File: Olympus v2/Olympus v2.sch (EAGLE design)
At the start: 170 parts, among them J1 HEADER_10P_0.05, Q1 BSS138, Q10 BSS138, Q11 BSS138, Q12 BSS138, Q2 BSS138, Q3 BSS138, Q4 BSS138, Q5 BSS138, Q6 BSS138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

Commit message: I updated Olympus by changing the USB pins, the GPIO LEDS, and updated the Hermes, Hephaestus, and Iris pinouts and connections to the microcontroller.  I also added pull down resistors on theLEDS.
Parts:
- removed JP63, JP64, JP65, JP71: (no value), pinhead:PINHD-1X2
- removed LED10, LED11, LED12, LED9: (no value), led:LEDCHIP-LED0603
- removed Q10, Q11, Q12, Q9: BSS138, transistor-small-signal:BSS123
- removed R11, R12, R13, R20: 100, resistor:R-US_R0603
- added JP88: (no value), pinhead:PINHD-1X2
- added R24, R25, R26, R27, R32, R33, R34, R35: 10k, resistor:R-US_R0603
- R10, R3, R4, R5, R6, R7, R8, R9: value 100 -> 1k
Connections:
- removed net HEPHAESTUS_GPIO: JP32.1, SV9.9
- removed net HERA_SONAR6: JP42.2, SV12.2
- removed net LED10_A: LED10.A, R12.1
- removed net LED10_C: LED10.C, Q10.D
- removed net LED10_G: JP64.1, Q10.G
- removed net LED11_A: LED11.A, R13.1
- removed net LED11_C: LED11.C, Q11.D
- removed net LED11_G: JP65.1, Q11.G
- removed net LED12_A: LED12.A, R20.1
- removed net LED12_C: LED12.C, Q12.D
- removed net LED12_G: JP71.1, Q12.G
- removed net LED9_A: LED9.A, R11.1
- removed net LED9_C: LED9.C, Q9.D
- removed net LED9_G: JP63.1, Q9.G
- removed net OLYMPUS_GPIO10: JP41.2, JP64.2
- removed net OLYMPUS_GPIO11: JP49.2, JP65.2
- removed net OLYMPUS_GPIO12: JP70.2, JP71.2
- removed net OLYMPUS_GPIO9: JP40.2, JP63.2
- new net ENABLE: SV7.7
- new net HEPH_BRAKE_DIR: JP21.1
- new net HEPH_BRAKE_DIR2: JP40.2
- new net HEPH_DIR_B: SV10.1
- new net HEPH_DIR_S: SV9.7
- new net HEPH_FAULT_B: JP38.2, SV10.4
- new net HEPH_FAULT_S: JP37.2, SV9.10
- new net HEPH_GPIO_B: SV10.3
- new net HEPH_GPIO_S: SV9.9
- new net HEPH_PWM_B: SV10.2
- new net HEPH_PWM_BRAKE: JP8.1
- new net HEPH_PWM_S: SV9.8
- new net HEPH_STR_DIR2: JP41.2
- new net HERMES_PED_DET: JP5.1, SV7.8
- new net IRIS_CLOCK: JP6.1, SV3.10
- new net IRIS_DATA: JP22.1, SV3.9
- new net N$2: JP88.2
- new net OLYMPUS_USBDM: JP31.1
- new net OLYMP_JTAG_SWO: JP20.1
- net DIONYSUS_BRD_EN: no longer JP18.1
- net GND: now also R24.2, R25.2, R26.2, R27.2, R32.2, R33.2, R34.2, R35.2; no longer Q10.S, Q11.S, Q12.S, Q9.S
- net HEPHAESTUS_DIR: no longer SV9.7
- net HEPHAESTUS_SPD: no longer SV9.8
- net HERA_HALL2: now also JP42.2; no longer JP31.1
- net HERMES_AUTOMAN: no longer SV7.7
- net LED1_G: now also R24.1
- net LED2_G: now also R25.1
- net LED3_G: now also R26.1
- net LED4_G: now also R27.1
- net LED5_G: now also R32.1
- net LED6_G: now also R33.1
- net LED7_G: now also R34.1
- net LED8_G: now also R35.1
- net MCU_BOOT0: now also JP88.1
- net OLYMPUS_GPIO1: now also JP11.1; no longer JP5.1
- net OLYMPUS_GPIO2: now also JP12.1; no longer JP6.1
- net OLYMPUS_GPIO3: now also JP13.1; no longer JP8.1
- net OLYMPUS_GPIO4: now also JP18.1; no longer JP20.1
- net OLYMPUS_GPIO5: now also JP49.2; no longer JP21.1
- net OLYMPUS_GPIO6: now also JP70.2; no longer JP22.1
- net OLYMPUS_GPIO7: no longer JP37.2
- net OLYMPUS_GPIO8: no longer JP38.2
- net OLYMPUS_USBDN: no longer JP12.1
- net OLYMPUS_USBDP: now also JP32.1; no longer JP13.1
- net OLYMPUS_USBID: no longer JP11.1
- net PP5V: no longer R11.2, R12.2, R13.2, R20.2
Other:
- moved on the sheet: JP55, JP56, JP57, JP58, JP59, JP60, JP61, JP62, LED1, LED2, LED3, LED4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

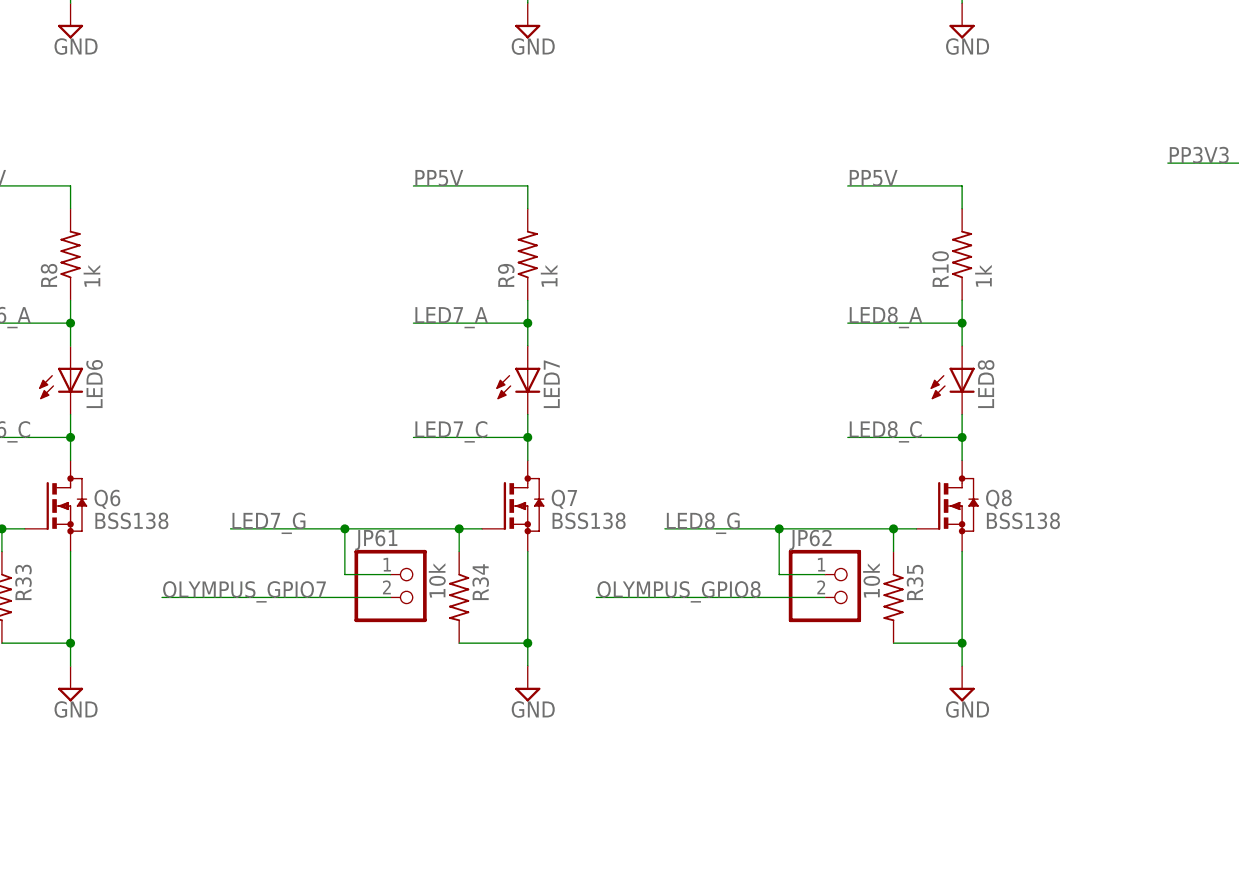
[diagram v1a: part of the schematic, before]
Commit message: I updated Olympus by changing the USB pins, the GPIO LEDS, and updated the Hermes, Hephaestus, and Iris pinouts and connections to the microcontroller.  I also added pull down resistors on theLEDS.
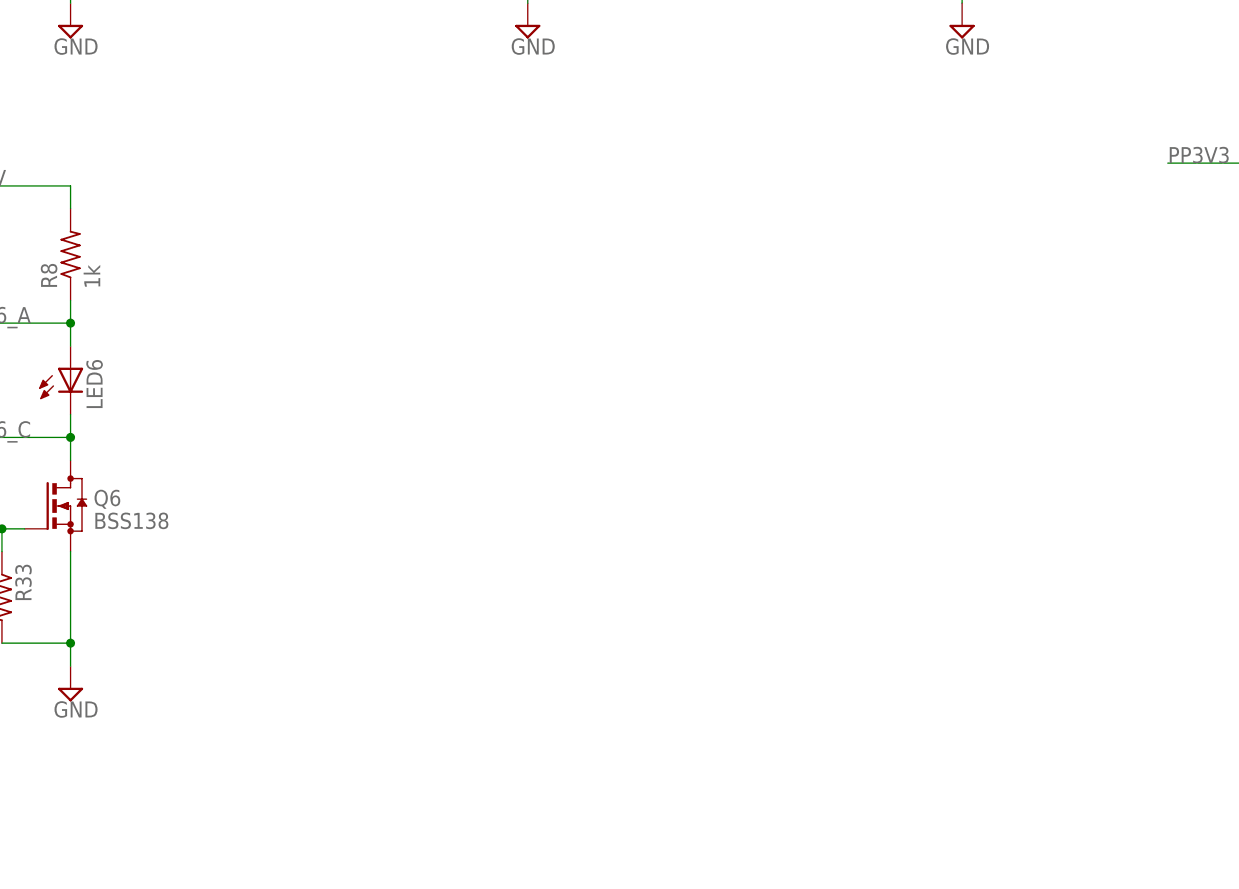
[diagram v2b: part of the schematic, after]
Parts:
- removed JP61, JP62: (no value), pinhead:PINHD-1X2
- removed LED7, LED8: (no value), led:LEDCHIP-LED0603
- removed Q7, Q8: BSS138, transistor-small-signal:BSS123
- removed R10, R9: 1k, resistor:R-US_R0603
- removed R34, R35: 10k, resistor:R-US_R0603
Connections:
- removed net LED7_A: LED7.A, R9.1
- removed net LED7_C: LED7.C, Q7.D
- removed net LED7_G: JP61.1, Q7.G, R34.1
- removed net LED8_A: LED8.A, R10.1
- removed net LED8_C: LED8.C, Q8.D
- removed net LED8_G: JP62.1, Q8.G, R35.1
- removed net OLYMPUS_GPIO7: JP61.2
- removed net OLYMPUS_GPIO8: JP62.2
- net GND: no longer Q7.S, Q8.S, R34.2, R35.2
- net PP5V: no longer R10.2, R9.2
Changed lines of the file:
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@@
 <part name="SUPPLY24" library="supply2" deviceset="GND" device=""/>
 <part name="JP60" library="pinhead" deviceset="PINHD-1X2" device=""/>
-<part name="LED7" library="led" deviceset="LED" device="CHIP-LED0603">
-<attribute name="DIGI" value="732-4966-1-ND"/>
-</part>
-<part name="R9" library="resistor" deviceset="R-US_" device="R0603" value="1k"/>
-<part name="Q7" library="transistor-small-signal" deviceset="BSS123" device="" value="BSS138">
-<attribute name="DIGI" value="BSS138CT-ND"/>
-</part>
-<part name="SUPPLY25" library="supply2" deviceset="GND" device=""/>
-<part name="JP61" library="pinhead" deviceset="PINHD-1X2" device=""/>
-<part name="LED8" library="led" deviceset="LED" device="CHIP-LED0603">
-<attribute name="DIGI" value="732-4966-1-ND"/>
-</part>
-<part name="R10" library="resistor" deviceset="R-US_" device="R0603" value="1k"/>
-<part name="Q8" library="transistor-small-signal" deviceset="BSS123" device="" value="BSS138">
-<attribute name="DIGI" value="BSS138CT-ND"/>
-</part>
-<part name="SUPPLY26" library="supply2" deviceset="GND" device=""/>
-<part name="JP62" library="pinhead" deviceset="PINHD-1X2" device=""/>
 <part name="L1" library="rcl" deviceset="L-US" device="L0201">
 <attribute name="DIGI" value="445-15755-1-ND"/>
@@
 <part name="R32" library="resistor" deviceset="R-US_" device="R0603" value="10k"/>
 <part name="R33" library="resistor" deviceset="R-US_" device="R0603" value="10k"/>
-<part name="R34" library="resistor" deviceset="R-US_" device="R0603" value="10k"/>
-<part name="R35" library="resistor" deviceset="R-US_" device="R0603" value="10k"/>
 <part name="U$1" library="Olympus" deviceset="NC" device=""/>
 </parts>
@@
 <instance part="SUPPLY24" gate="GND" x="454.66" y="190.5"/>
 <instance part="JP60" gate="G$1" x="441.96" y="200.66"/>
-<instance part="LED7" gate="G$1" x="505.46" y="226.06">
-<attribute name="DIGI" x="505.46" y="226.06" size="1.778" layer="96" display="off"/>
-</instance>
-<instance part="R9" gate="G$1" x="505.46" y="238.76" rot="R90"/>
-<instance part="Q7" gate="G$1" x="505.46" y="210.82">
-<attribute name="DIGI" x="505.46" y="210.82" size="1.778" layer="96" display="off"/>
-</instance>
-<instance part="SUPPLY25" gate="GND" x="505.46" y="190.5"/>
-<instance part="JP61" gate="G$1" x="492.76" y="200.66"/>
-<instance part="LED8" gate="G$1" x="553.72" y="226.06">
-<attribute name="DIGI" x="553.72" y="226.06" size="1.778" layer="96" display="off"/>
-</instance>
-<instance part="R10" gate="G$1" x="553.72" y="238.76" rot="R90"/>
-<instance part="Q8" gate="G$1" x="553.72" y="210.82">
-<attribute name="DIGI" x="553.72" y="210.82" size="1.778" layer="96" display="off"/>
-</instance>
-<instance part="SUPPLY26" gate="GND" x="553.72" y="190.5"/>
-<instance part="JP62" gate="G$1" x="541.02" y="200.66"/>
 <instance part="L1" gate="G$1" x="259.08" y="68.58" rot="R90">
 <attribute name="DIGI" x="259.08" y="68.58" size="1.778" layer="96" rot="R90" display="off"/>
@@
 <instance part="R32" gate="G$1" x="393.7" y="200.66" rot="R270"/>
 <instance part="R33" gate="G$1" x="447.04" y="200.66" rot="R270"/>
-<instance part="R34" gate="G$1" x="497.84" y="200.66" rot="R270"/>
-<instance part="R35" gate="G$1" x="546.1" y="200.66" rot="R270"/>
 <instance part="U$1" gate="G$1" x="523.24" y="43.18"/>
 </instances>
@@
 <wire x1="325.12" y1="160.02" x2="355.6" y2="160.02" width="0.1524" layer="91"/>
 <label x="355.6" y="160.02" size="1.778" layer="95" rot="MR0"/>
-</segment>
-</net>
-<net name="OLYMPUS_GPIO7" class="0">
-<segment>
-<pinref part="JP61" gate="G$1" pin="2"/>
-<wire x1="490.22" y1="200.66" x2="464.82" y2="200.66" width="0.1524" layer="91"/>
-<label x="464.82" y="200.66" size="1.778" layer="95"/>
-</segment>
-</net>
-<net name="OLYMPUS_GPIO8" class="0">
-<segment>
-<pinref part="JP62" gate="G$1" pin="2"/>
-<wire x1="538.48" y1="200.66" x2="513.08" y2="200.66" width="0.1524" layer="91"/>
-<label x="513.08" y="200.66" size="1.778" layer="95"/>
 </segment>
 </net>
@@
 <wire x1="447.04" y1="195.58" x2="454.66" y2="195.58" width="0.1524" layer="91"/>
 <junction x="454.66" y="195.58"/>
-</segment>
-<segment>
-<pinref part="Q7" gate="G$1" pin="S"/>
-<wire x1="505.46" y1="205.74" x2="505.46" y2="195.58" width="0.1524" layer="91"/>
-<pinref part="SUPPLY25" gate="GND" pin="GND"/>
-<pinref part="R34" gate="G$1" pin="2"/>
-<wire x1="505.46" y1="195.58" x2="505.46" y2="193.04" width="0.1524" layer="91"/>
-<wire x1="497.84" y1="195.58" x2="505.46" y2="195.58" width="0.1524" layer="91"/>
-<junction x="505.46" y="195.58"/>
-</segment>
-<segment>
-<pinref part="Q8" gate="G$1" pin="S"/>
-<wire x1="553.72" y1="205.74" x2="553.72" y2="195.58" width="0.1524" layer="91"/>
-<pinref part="SUPPLY26" gate="GND" pin="GND"/>
-<pinref part="R35" gate="G$1" pin="2"/>
-<wire x1="553.72" y1="195.58" x2="553.72" y2="193.04" width="0.1524" layer="91"/>
-<wire x1="546.1" y1="195.58" x2="553.72" y2="195.58" width="0.1524" layer="91"/>
-<junction x="553.72" y="195.58"/>
 </segment>
 <segment>
@@
 </segment>
 <segment>
-<pinref part="R10" gate="G$1" pin="2"/>
-<wire x1="553.72" y1="243.84" x2="553.72" y2="246.38" width="0.1524" layer="91"/>
-<wire x1="553.72" y1="246.38" x2="541.02" y2="246.38" width="0.1524" layer="91"/>
-<label x="541.02" y="246.38" size="1.778" layer="95"/>
-</segment>
-<segment>
-<pinref part="R9" gate="G$1" pin="2"/>
-<wire x1="505.46" y1="243.84" x2="505.46" y2="246.38" width="0.1524" layer="91"/>
-<wire x1="505.46" y1="246.38" x2="492.76" y2="246.38" width="0.1524" layer="91"/>
-<label x="492.76" y="246.38" size="1.778" layer="95"/>
-</segment>
-<segment>
 <pinref part="R8" gate="G$1" pin="2"/>
 <wire x1="454.66" y1="243.84" x2="454.66" y2="246.38" width="0.1524" layer="91"/>
@@
 </segment>
 </net>
-<net name="LED7_A" class="0">
-<segment>
-<pinref part="LED7" gate="G$1" pin="A"/>
-<pinref part="R9" gate="G$1" pin="1"/>
-<wire x1="505.46" y1="233.68" x2="505.46" y2="231.14" width="0.1524" layer="91"/>
-<wire x1="505.46" y1="231.14" x2="505.46" y2="228.6" width="0.1524" layer="91"/>
-<wire x1="505.46" y1="231.14" x2="492.76" y2="231.14" width="0.1524" layer="91"/>
-<junction x="505.46" y="231.14"/>
-<label x="492.76" y="231.14" size="1.778" layer="95"/>
-</segment>
-</net>
-<net name="LED7_C" class="0">
-<segment>
-<pinref part="LED7" gate="G$1" pin="C"/>
-<wire x1="505.46" y1="220.98" x2="505.46" y2="218.44" width="0.1524" layer="91"/>
-<wire x1="505.46" y1="218.44" x2="492.76" y2="218.44" width="0.1524" layer="91"/>
-<pinref part="Q7" gate="G$1" pin="D"/>
-<wire x1="505.46" y1="218.44" x2="505.46" y2="215.9" width="0.1524" layer="91"/>
-<junction x="505.46" y="218.44"/>
-<label x="492.76" y="218.44" size="1.778" layer="95"/>
-</segment>
-</net>
-<net name="LED7_G" class="0">
-<segment>
-<pinref part="Q7" gate="G$1" pin="G"/>
-<wire x1="500.38" y1="208.28" x2="497.84" y2="208.28" width="0.1524" layer="91"/>
-<pinref part="JP61" gate="G$1" pin="1"/>
-<wire x1="497.84" y1="208.28" x2="485.14" y2="208.28" width="0.1524" layer="91"/>
-<wire x1="485.14" y1="208.28" x2="472.44" y2="208.28" width="0.1524" layer="91"/>
-<wire x1="490.22" y1="203.2" x2="485.14" y2="203.2" width="0.1524" layer="91"/>
-<wire x1="485.14" y1="203.2" x2="485.14" y2="208.28" width="0.1524" layer="91"/>
-<junction x="485.14" y="208.28"/>
-<label x="472.44" y="208.28" size="1.778" layer="95"/>
-<pinref part="R34" gate="G$1" pin="1"/>
-<wire x1="497.84" y1="205.74" x2="497.84" y2="208.28" width="0.1524" layer="91"/>
-<junction x="497.84" y="208.28"/>
-</segment>
-</net>
-<net name="LED8_A" class="0">
-<segment>
-<pinref part="LED8" gate="G$1" pin="A"/>
-<pinref part="R10" gate="G$1" pin="1"/>
-<wire x1="553.72" y1="233.68" x2="553.72" y2="231.14" width="0.1524" layer="91"/>
-<wire x1="553.72" y1="231.14" x2="553.72" y2="228.6" width="0.1524" layer="91"/>
-<wire x1="553.72" y1="231.14" x2="541.02" y2="231.14" width="0.1524" layer="91"/>
-<junction x="553.72" y="231.14"/>
-<label x="541.02" y="231.14" size="1.778" layer="95"/>
-</segment>
-</net>
-<net name="LED8_C" class="0">
-<segment>
-<pinref part="LED8" gate="G$1" pin="C"/>
-<wire x1="553.72" y1="220.98" x2="553.72" y2="218.44" width="0.1524" layer="91"/>
-<wire x1="553.72" y1="218.44" x2="541.02" y2="218.44" width="0.1524" layer="91"/>
-<pinref part="Q8" gate="G$1" pin="D"/>
-<wire x1="553.72" y1="218.44" x2="553.72" y2="215.9" width="0.1524" layer="91"/>
-<junction x="553.72" y="218.44"/>
-<label x="541.02" y="218.44" size="1.778" layer="95"/>
-</segment>
-</net>
-<net name="LED8_G" class="0">
-<segment>
-<pinref part="Q8" gate="G$1" pin="G"/>
-<wire x1="548.64" y1="208.28" x2="546.1" y2="208.28" width="0.1524" layer="91"/>
-<pinref part="JP62" gate="G$1" pin="1"/>
-<wire x1="546.1" y1="208.28" x2="533.4" y2="208.28" width="0.1524" layer="91"/>
-<wire x1="533.4" y1="208.28" x2="520.7" y2="208.28" width="0.1524" layer="91"/>
-<wire x1="538.48" y1="203.2" x2="533.4" y2="203.2" width="0.1524" layer="91"/>
-<wire x1="533.4" y1="203.2" x2="533.4" y2="208.28" width="0.1524" layer="91"/>
-<junction x="533.4" y="208.28"/>
-<label x="520.7" y="208.28" size="1.778" layer="95"/>
-<pinref part="R35" gate="G$1" pin="1"/>
-<wire x1="546.1" y1="205.74" x2="546.1" y2="208.28" width="0.1524" layer="91"/>
-<junction x="546.1" y="208.28"/>
-</segment>
-</net>
